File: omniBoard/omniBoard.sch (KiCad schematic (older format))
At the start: 17 parts

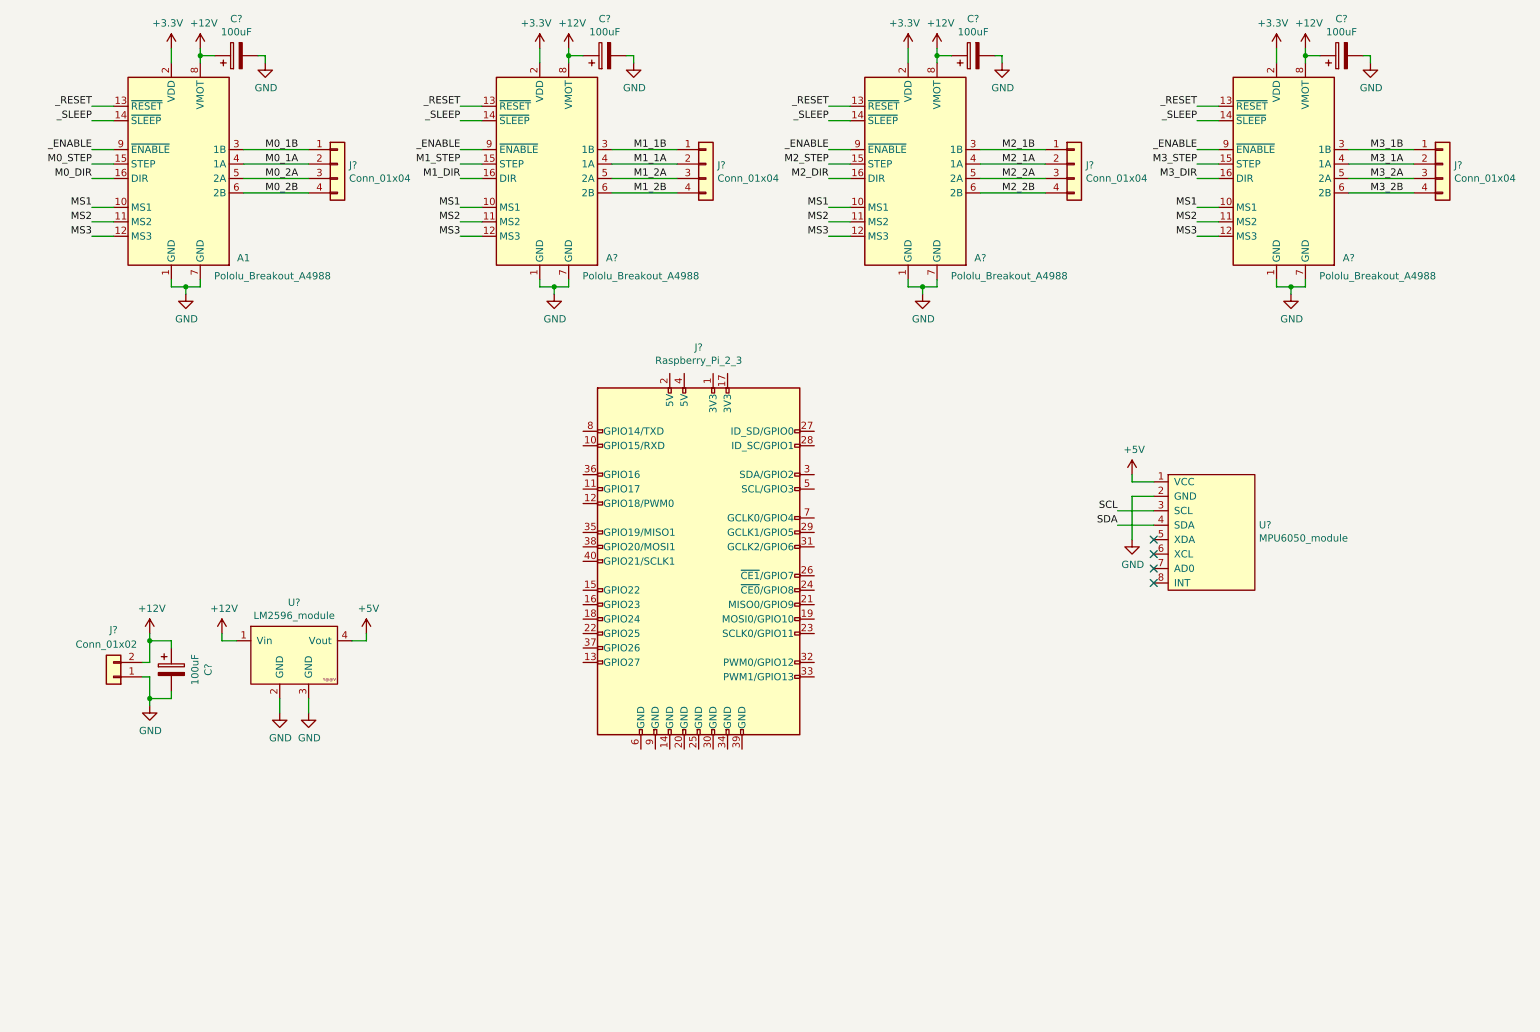
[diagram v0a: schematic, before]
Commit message: Add footprints and ADC
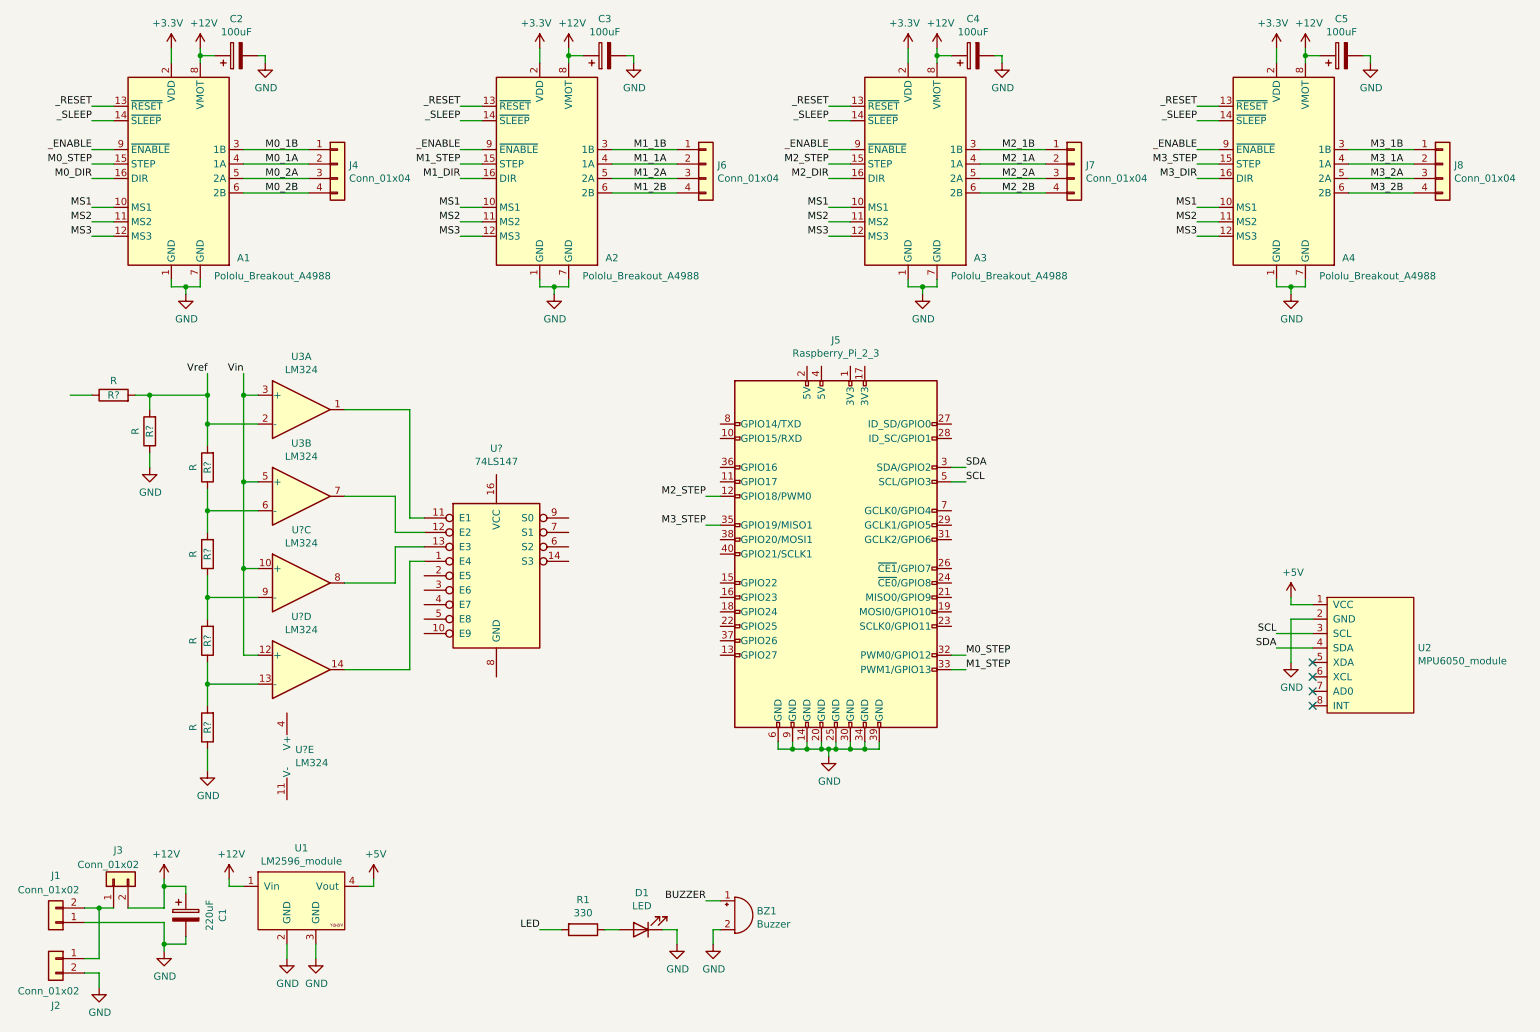
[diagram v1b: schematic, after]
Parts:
- removed U?: LM2596_module, symbol omniBoard:LM2596_module
- removed U?: MPU6050_module, symbol omniBoard:MPU6050_module
- added BZ1: Buzzer, Buzzer_Beeper:Buzzer_12x9.5RM7.6, symbol Device:Buzzer
- added D1: LED, LED_THT:LED_D5.0mm, symbol Device:LED
- added J2, J3: Conn_01x02, TerminalBlock_Phoenix:TerminalBlock_Phoenix_MKDS-1,5-2_1x02_P5.00mm_Horizontal, symbol Connector_Generic:Conn_01x02
- added R1: 330, Resistor_THT:R_Axial_DIN0309_L9.0mm_D3.2mm_P15.24mm_Horizontal, symbol Device:R
- added R? (x6): R, Resistor_THT:R_Axial_DIN0309_L9.0mm_D3.2mm_P15.24mm_Horizontal, symbol Device:R
- added U1: LM2596_module, omniBoard:LM2596_module, symbol omniBoard:LM2596_module
- added U2: MPU6050_module, omniBoard:MPU6050_module, symbol omniBoard:MPU6050_module
- added U3, U? (x3): LM324, Package_DIP:DIP-14_W7.62mm, symbol Amplifier_Operational:LM324
- added U?: 74LS147, Package_DIP:DIP-16_W7.62mm, symbol 74xx:74LS147
- C1: renamed from C?; value 100uF -> 220uF; footprint (none) -> Capacitor_THT:CP_Radial_D8.0mm_P3.50mm
- C2, C3, C4, C5: renamed from C?; footprint (none) -> Capacitor_THT:CP_Radial_D6.3mm_P2.50mm
- J4, J6, J7, J8: renamed from J?; footprint (none) -> Connector_PinHeader_2.54mm:PinHeader_1x04_P2.54mm_Vertical
- gave numbers to parts that had none: 5
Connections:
- net +12V: now also J3.2 (Pin_2), U1.1 (Vin); no longer J1.2 (Pin_2)
- net +5V: now also U1.4 (Vout), U2.1 (VCC)
- net GND: now also J5.14 (GND), J5.20 (GND), J5.25 (GND), J5.30 (GND), J5.34 (GND), J5.39 (GND), J5.6 (GND), J5.9 (GND), BZ1.2 (+), D1.1 (K), J2.2 (Pin_2), R?.1, R?.1, U1.2 (GND), U1.3 (GND), U2.2 (GND)
- net M0_STEP: now also J5.32 (PWM0/GPIO12)
- net M1_STEP: now also J5.33 (PWM1/GPIO13)
- net M2_STEP: now also J5.12 (GPIO18/PWM0)
- net M3_STEP: now also J5.35 (GPIO19/MISO1)
- net SCL: now also J5.5 (SCL/GPIO3), U2.3 (SCL)
- net SDA: now also J5.3 (SDA/GPIO2), U2.4 (SDA)
- new net: U3.1, U?.11 (E1)
- new net: R?.1, R?.2, U3.6 (-)
- new net: U3.7, U?.12 (E2)
- new net: J1.2 (Pin_2), J2.1 (Pin_1), J3.1 (Pin_1)
- new net: U?.13 (E3), U?.8
- new net: R?.1, R?.2, U?.9 (-)
- new net: R?.1, R?.2, U?.13 (-)
- new net: U?.1 (E4), U?.14
- new net: D1.2 (A), R1.1
- new net BUZZER: BZ1.1 (-)
- new net LED: R1.2
- new net Vin: U3.3 (+), U3.5 (+), U?.10 (+), U?.12 (+)
- new net Vref: R?.2, R?.2, R?.2, U3.2 (-)
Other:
- moved on the sheet: C1, J1, J5

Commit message: Place components on the board
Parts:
- R1, R2, R3, R4, R5, R6: renamed from R?; footprint Resistor_THT:R_Axial_DIN0309_L9.0mm_D3.2mm_P15.24mm_Horizontal -> Resistor_THT:R_Axial_DIN0207_L6.3mm_D2.5mm_P10.16mm_Horizontal
- R7: renamed from R1; footprint Resistor_THT:R_Axial_DIN0309_L9.0mm_D3.2mm_P15.24mm_Horizontal -> Resistor_THT:R_Axial_DIN0207_L6.3mm_D2.5mm_P10.16mm_Horizontal
- gave numbers to parts that had none: 2
- renumbered J6 to J5, J5 to J6, U3 to U1, U1 to U2, U2 to U4

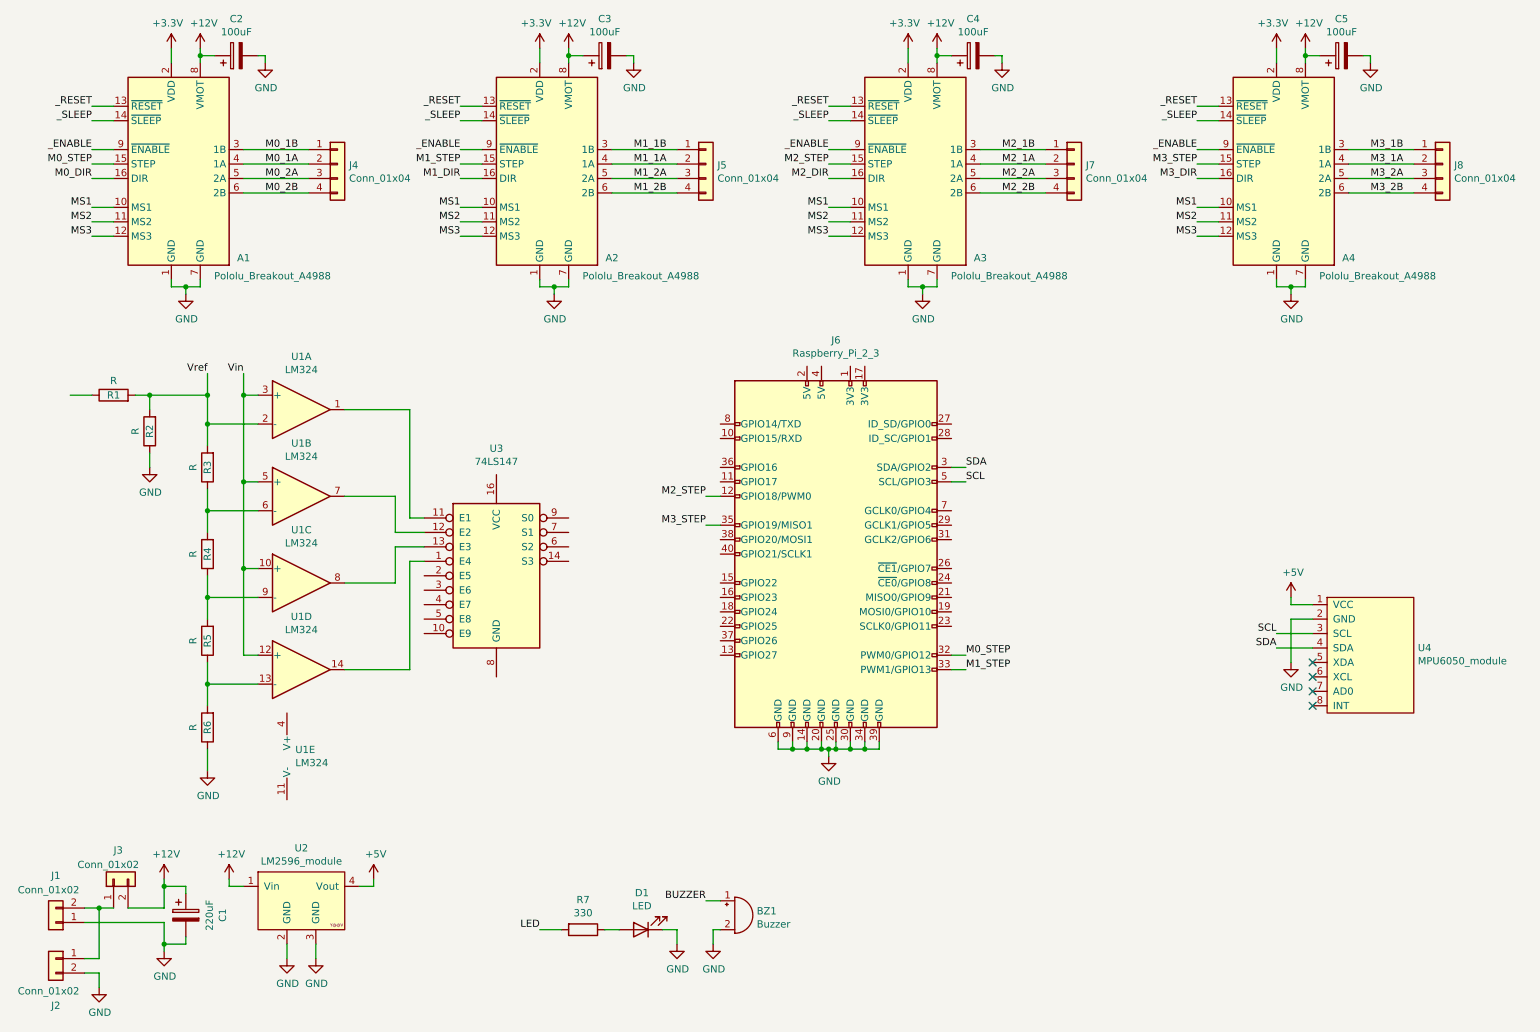
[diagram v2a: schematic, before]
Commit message: Remove useless components
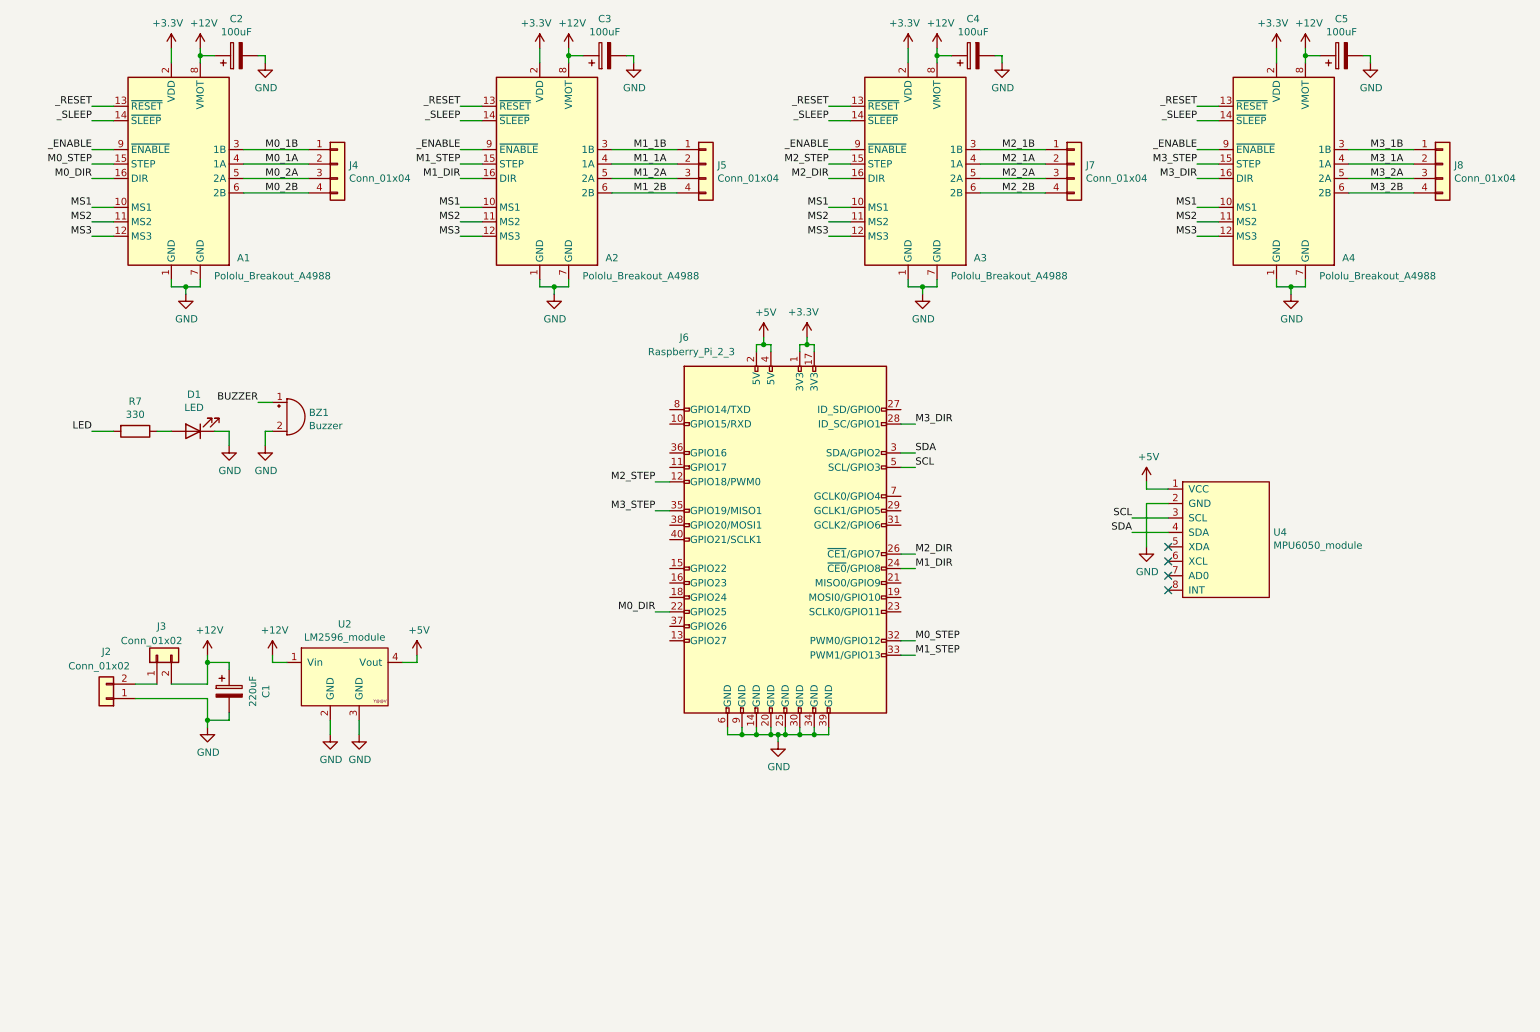
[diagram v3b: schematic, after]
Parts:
- removed J1: Conn_01x02, Connector_AMASS:AMASS_XT60-F_1x02_P7.20mm_Vertical, symbol Connector_Generic:Conn_01x02
- removed R1, R2, R3, R4, R5, R6: R, Resistor_THT:R_Axial_DIN0207_L6.3mm_D2.5mm_P10.16mm_Horizontal, symbol Device:R
- removed U1: LM324, Package_DIP:DIP-14_W7.62mm, symbol Amplifier_Operational:LM324
- removed U3: 74LS147, Package_DIP:DIP-16_W7.62mm, symbol 74xx:74LS147
- J3: footprint TerminalBlock_Phoenix:TerminalBlock_Phoenix_MKDS-1,5-2_1x02_P5.00mm_Horizontal -> TerminalBlock_Phoenix:TerminalBlock_Phoenix_MKDS-1,5-2-5.08_1x02_P5.08mm_Horizontal
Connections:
- net +3V3: now also J6.1 (3V3), J6.17 (3V3)
- net +5V: now also J6.2 (5V), J6.4 (5V)
- net GND: now also J2.1 (Pin_1); no longer J2.2 (Pin_2)
- net M0_DIR: now also J6.22 (GPIO25)
- net M1_DIR: now also J6.24 (~CE0~/GPIO8)
- net M2_DIR: now also J6.26 (~CE1~/GPIO7)
- net M3_DIR: now also J6.28 (ID_SC/GPIO1)
- net at J3.1 (Pin_1): now also J2.2 (Pin_2); no longer J2.1 (Pin_1)
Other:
- moved on the sheet: BZ1, C1, D1, J2, J3, J6, R7, U2, U4

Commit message: Finish board 1st version
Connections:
- net MS1 is gone; now on net +3V3: A1.10 (MS1), A2.10 (MS1), A3.10 (MS1), A4.10 (MS1)
- net MS2 is gone; now on net +3V3: A1.11 (MS2), A2.11 (MS2), A3.11 (MS2), A4.11 (MS2)
- net MS3 is gone; now on net +3V3: A1.12 (MS3), A2.12 (MS3), A3.12 (MS3), A4.12 (MS3)
- net +3V3: now also U4.1 (VCC)
- net +5V: no longer U4.1 (VCC)
- net BUZZER: now also J6.7 (GCLK0/GPIO4)
- net LED: now also J6.11 (GPIO17)
- net M0_DIR: now also J6.31 (GCLK2/GPIO6); no longer J6.22 (GPIO25)
- net M0_STEP: now also J6.33 (PWM1/GPIO13); no longer J6.32 (PWM0/GPIO12)
- net M1_DIR: now also J6.38 (GPIO20/MOSI1); no longer J6.24 (~CE0~/GPIO8)
- net M1_STEP: now also J6.35 (GPIO19/MISO1); no longer J6.33 (PWM1/GPIO13)
- net M2_DIR: now also J6.36 (GPIO16); no longer J6.26 (~CE1~/GPIO7)
- net M2_STEP: now also J6.32 (PWM0/GPIO12); no longer J6.12 (GPIO18/PWM0)
- net M3_DIR: now also J6.16 (GPIO23); no longer J6.28 (ID_SC/GPIO1)
- net M3_STEP: now also J6.12 (GPIO18/PWM0); no longer J6.35 (GPIO19/MISO1)
- removed net _RESET: A1.13 (~RESET), A2.13 (~RESET), A3.13 (~RESET), A4.13 (~RESET)
- removed net _SLEEP: A1.14 (~SLEEP), A2.14 (~SLEEP), A3.14 (~SLEEP), A4.14 (~SLEEP)
- new net _RESET0: A1.13 (~RESET), A1.14 (~SLEEP)
- new net _RESET1: A2.13 (~RESET), A2.14 (~SLEEP)
- new net _RESET2: A3.13 (~RESET), A3.14 (~SLEEP)
- new net _RESET3: A4.13 (~RESET), A4.14 (~SLEEP)
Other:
- moved on the sheet: BZ1, C1, D1, J2, J3, R7, U2, U4
